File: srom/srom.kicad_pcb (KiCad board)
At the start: 2 copper layers, 83.3 x 76.1 mm, 31 parts, among them J1 Conn_01x03_Female, Q1 PN2222A, SW1 SW_SPST, U1 4075, U2 74LS245, U3 74LS245, U4 74LS245, U5 Pico-rp2040

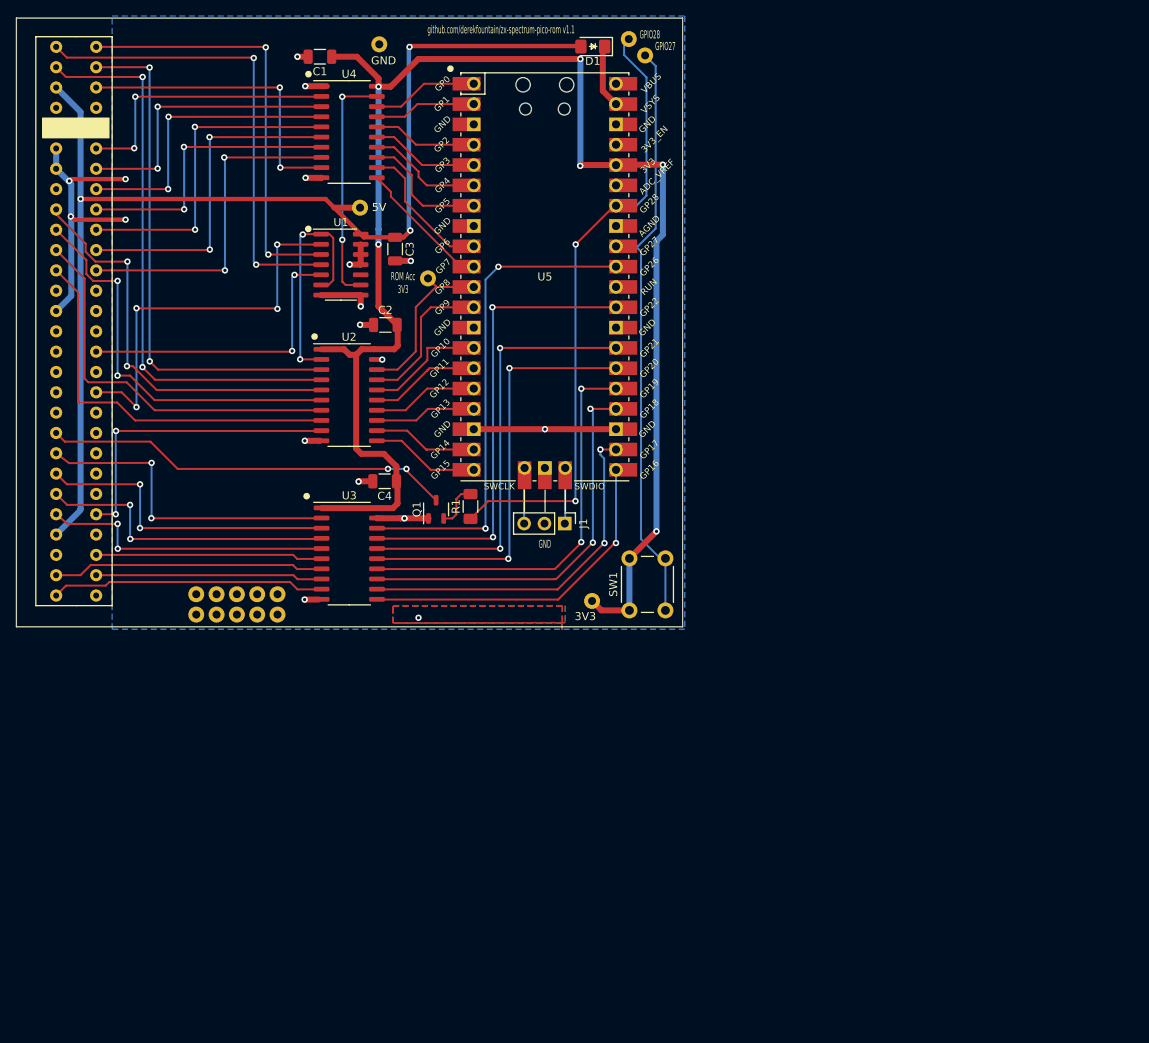
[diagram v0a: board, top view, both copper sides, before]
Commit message: first draft pcb layout
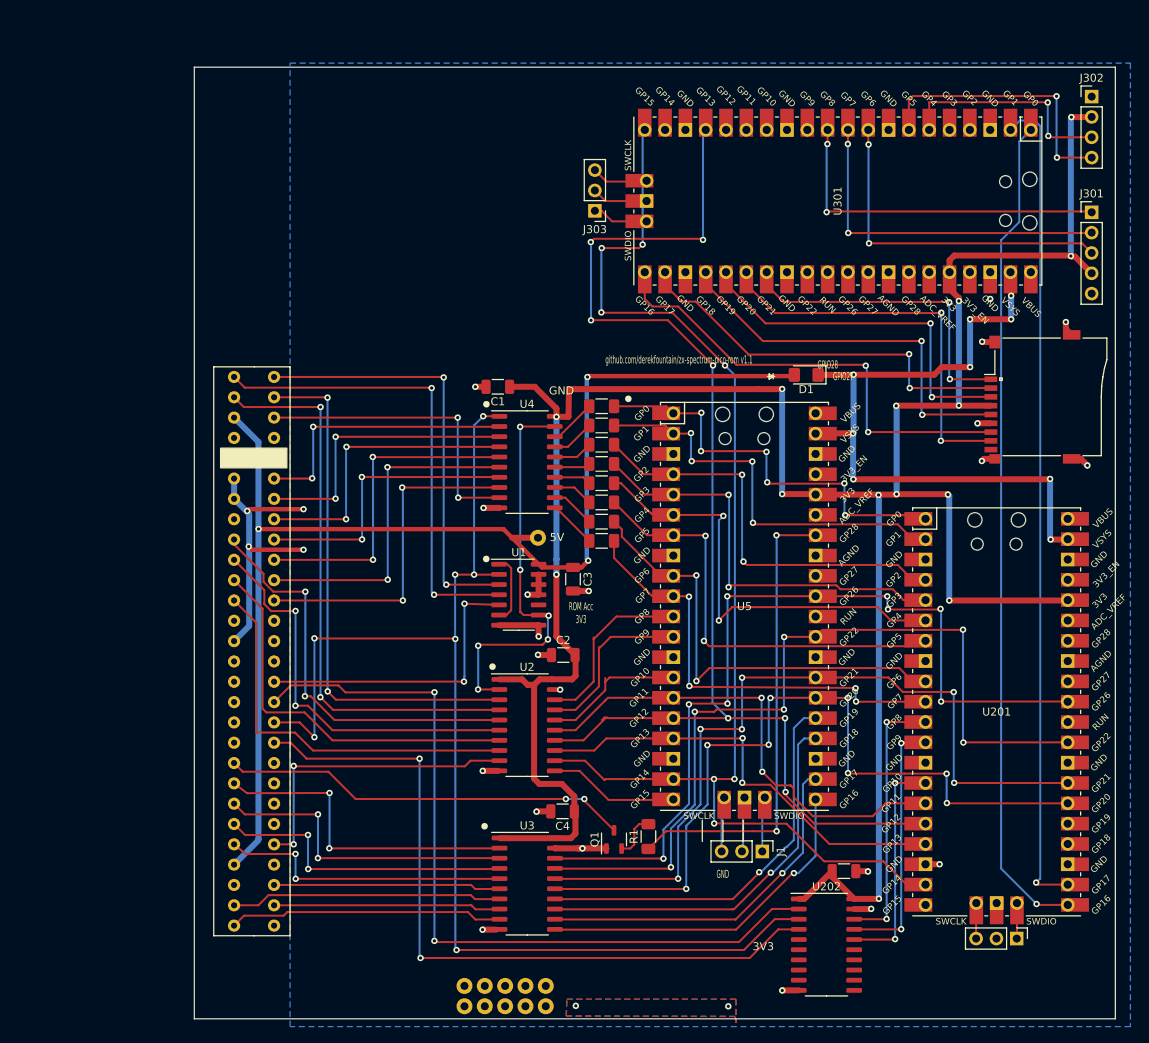
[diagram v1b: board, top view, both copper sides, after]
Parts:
- removed the 14 at (95.1, 122.8)
- removed the 14 at (68.5, 53.3)
- removed the ? at (101.8, 54.6)
- removed the ? at (99.7, 52.6)
- removed the ? at (74.6, 82.5)
- removed SW1: SW_SPST, Button_Switch_THT:SW_PUSH_6mm_H4.3mm
- added C201: C_Small, Capacitor_SMD:C_1206_3216Metric, F.Cu at (126.6, 156.6)
- added J201: Conn_01x03_Female, Connector_PinHeader_2.54mm:PinHeader_1x03_P2.54mm_Vertical, F.Cu at (148.2, 165.0)
- added J301: Conn_01x05_Female, Connector_PinHeader_2.54mm:PinHeader_1x05_P2.54mm_Vertical, F.Cu at (157.6, 74.3)
- added J302: Conn_01x04_Female, Connector_PinHeader_2.54mm:PinHeader_1x04_P2.54mm_Vertical, F.Cu at (157.6, 59.8)
- added J303: Conn_01x03_Female, Connector_PinHeader_2.54mm:PinHeader_1x03_P2.54mm_Vertical, F.Cu at (95.5, 74.1)
- added R101: R470, Resistor_SMD:R_1206_3216Metric_Pad1.30x1.75mm_HandSolder, F.Cu at (96.3, 98.5)
- added R102: R470, Resistor_SMD:R_1206_3216Metric_Pad1.30x1.75mm_HandSolder, F.Cu at (96.3, 100.9)
- added R103: R470, Resistor_SMD:R_1206_3216Metric_Pad1.30x1.75mm_HandSolder, F.Cu at (96.3, 103.3)
- added R104: R470, Resistor_SMD:R_1206_3216Metric_Pad1.30x1.75mm_HandSolder, F.Cu at (96.3, 105.7)
- added R105: R470, Resistor_SMD:R_1206_3216Metric_Pad1.30x1.75mm_HandSolder, F.Cu at (96.3, 108.1)
- added R106: R470, Resistor_SMD:R_1206_3216Metric_Pad1.30x1.75mm_HandSolder, F.Cu at (96.3, 110.5)
- added R107: R470, Resistor_SMD:R_1206_3216Metric_Pad1.30x1.75mm_HandSolder, F.Cu at (96.3, 112.9)
- added R108: R470, Resistor_SMD:R_1206_3216Metric_Pad1.30x1.75mm_HandSolder, F.Cu at (96.3, 115.3)
- added U201: Pico-2 IO, pico-foot:RPi_Pico_SMD_TH, F.Cu at (145.7, 136.7)
- added U202: 74LS245, Package_SO:SO-20_5.3x12.6mm_P1.27mm, F.Cu at (124.4, 165.8)
- added U301: Pico-3 UI, pico-foot:RPi_Pico_SMD_TH, F.Cu at (125.9, 72.8)
- added XS301: 502p_SD_ebay-uSD-push_push_SMD-pak_breakout, uSD:Conn_uSDcard, F.Cu at (155.5, 97.3)
- U5: value Pico-rp2040 -> Pico-1 ROM
- moved 5 59.3 mm to (79.2, 171.0)
- moved 6 59.3 mm to (81.7, 171.0)
- moved 8 59.3 mm to (86.8, 171.0)
- moved 7 59.3 mm to (84.3, 171.0)
- moved 9 59.3 mm to (89.3, 171.0)
- moved 10 59.3 mm to (79.2, 173.5)
- moved 11 59.3 mm to (81.7, 173.5)
- moved 12 59.3 mm to (84.3, 173.5)
- moved 13 59.3 mm to (86.8, 173.5)
- moved 14 59.3 mm to (89.3, 173.5)
- moved D1 49.0 mm to (121.9, 94.6)
- moved U5 48.2 mm to (114.2, 123.5)
- moved J1 47.8 mm to (116.4, 154.2)
- moved U2 46.9 mm to (87.0, 138.4)
- moved C3 46.9 mm to (92.8, 120.1)
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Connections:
- net Net-(D1-Pad1) renamed PICO_PWR
- net ROM_ACCESS_INV_3V3 renamed ROM_READ_INV_3V3
- net SWDCLK renamed SWDCLK_P1
- net SWDIO renamed SWDIO_P1
- U1 pad 11: GND -> unconnected-(U1-Pad11)
- U1 pad 12: GND -> unconnected-(U1-Pad12)
- U1 pad 13: GND -> unconnected-(U1-Pad13)
- U2 pad 2: ROM_ACCESS_INV -> ROM_READ_INV
- U4 pad 1: GND -> ZXRD
- U4 pad 11: D7 -> Net-(R108-Pad1)
- U4 pad 12: D4 -> Net-(R107-Pad1)
- U4 pad 13: D6 -> Net-(R106-Pad1)
- U4 pad 14: D3 -> Net-(R105-Pad1)
- U4 pad 15: D5 -> Net-(R104-Pad1)
- U4 pad 16: D2 -> Net-(R103-Pad1)
- U4 pad 17: D1 -> Net-(R102-Pad1)
- U4 pad 18: D0 -> Net-(R101-Pad1)
- U4 pad 19: ROM_READ_INV -> GND
- U5 pad 32: PICO_USER_INPUT -> unconnected-(U5-Pad32)
- Z1 pad A17: unconnected-(Z1-PadA17) -> ZXIORQ
- Z1 pad A19: unconnected-(Z1-PadA19) -> ZXWR
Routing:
- net A1: track 13.2 -> 160.8 mm, vias 0 -> 7
- net A3: track 13.2 -> 158.3 mm, vias 0 -> 7
- net +3V3: track 196.8 -> 321.7 mm, vias 6 -> 14
- net ZXRD: track 49.1 -> 155.4 mm, vias 4 -> 7
- net UI_PICO_TX: track 0.00 -> 104.1 mm, vias 0 -> 1
- net UI_PICO_RX: track 0.00 -> 103.3 mm, vias 0 -> 1
- net ZXIORQ: track 0.00 -> 99.7 mm, vias 0 -> 2
- net ZXWR: track 0.00 -> 92.9 mm, vias 0 -> 2
- net PICO_PWR: track 7.87 -> 88.6 mm, vias 0 -> 9
- net PICO_USER_INPUT: track 75.5 -> 0.00 mm
- net MISO_D0: track 0.00 -> 58.5 mm, vias 0 -> 2
- net SD_SS: track 0.00 -> 50.2 mm, vias 0 -> 2
- net SD_DAT1: track 0.00 -> 49.7 mm, vias 0 -> 2
- net SD_CLK: track 0.00 -> 49.3 mm, vias 0 -> 2
- net A4: track 53.6 -> 101.3 mm, vias 2 -> 8
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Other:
- board size 83.3 x 76.1 mm -> 115.1 x 118.9 mm

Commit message: design rules checker happy
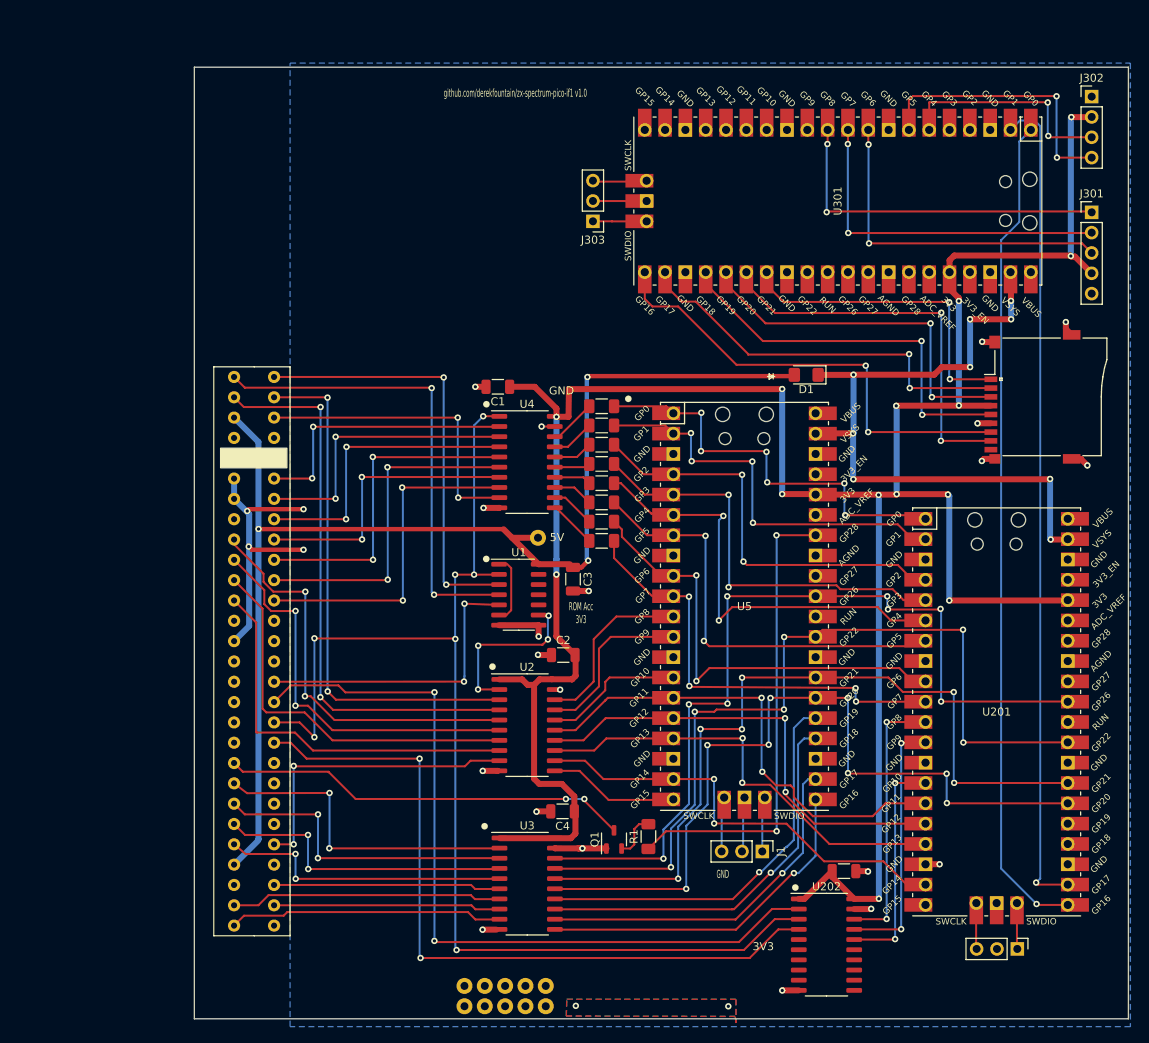
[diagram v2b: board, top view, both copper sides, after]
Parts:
- moved J303 1.33 mm to (95.2, 75.4)
- moved J201 1.30 mm to (148.3, 166.3)
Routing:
- net A3: track 158.3 -> 53.6 mm, vias 7 -> 2
- net A1: track 160.8 -> 58.5 mm, vias 7 -> 2
- net GND: track 122.4 -> 93.8 mm, vias 28 -> 26
- net unconnected-(U1-Pad12): track 3.92 -> 0.00 mm, vias 1 -> 0
- net D4: track 56.9 -> 53.7 mm
- net +3V3: track 321.7 -> 319.1 mm
- net A4: track 101.3 -> 99.4 mm
- net SD_SS: track 50.2 -> 48.6 mm
- net SD_DAT2: track 40.1 -> 38.5 mm
- net D2: track 52.2 -> 50.6 mm
- net D1: track 51.3 -> 49.7 mm
- net OLED_SDA: track 34.4 -> 32.9 mm
- net SD_DAT1: track 49.7 -> 48.2 mm
- net SD_CLK: track 49.3 -> 47.8 mm
- net MOSI_DI: track 45.7 -> 44.3 mm
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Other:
- board size 115.1 x 118.9 mm -> 116.8 x 118.9 mm
- board text added: "github.com/derekfountain/zx-spectrum-pico-if1 v1.0"
- board text removed: "GPIO27"
- board text removed: "GPIO28"
- board text removed: "github.com/derekfountain/zx-spectrum-pico-rom v1.1"

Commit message: ready for fab
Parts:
- added 10: , , F.Cu at (84.7, 92.5)
- added 10: , , F.Cu at (84.7, 87.6)
- added 10: , , F.Cu at (133.0, 173.3)
- added 10: , , F.Cu at (149.8, 173.3)
- added 10: , , F.Cu at (84.7, 82.5)
- added 11: , , F.Cu at (152.3, 173.3)
- added 11: , , F.Cu at (135.6, 173.3)
- added 11: , , F.Cu at (87.3, 87.6)
- added 11: , , F.Cu at (87.2, 82.5)
- added 11: , , F.Cu at (87.2, 92.5)
- added 12: , , F.Cu at (154.8, 173.3)
- added 12: , , F.Cu at (89.8, 82.5)
- added 12: , , F.Cu at (138.1, 173.3)
- added 12: , , F.Cu at (89.8, 87.6)
- added 12: , , F.Cu at (89.8, 92.5)
- added 13: , , F.Cu at (92.3, 87.6)
- added 13: , , F.Cu at (157.4, 173.3)
- added 13: , , F.Cu at (92.3, 92.5)
- added 13: , , F.Cu at (140.6, 173.3)
- added 13: , , F.Cu at (92.3, 82.5)
- added 14: , , F.Cu at (94.8, 82.5)
- added 14: , , F.Cu at (94.8, 92.5)
- added 14: , , F.Cu at (94.9, 87.6)
- added 14: , , F.Cu at (143.2, 173.3)
- added 14: , , F.Cu at (159.9, 173.3)
- added 5: , , F.Cu at (84.7, 90.0)
- added 5: , , F.Cu at (149.8, 170.7)
- added 5: , , F.Cu at (133.0, 170.8)
- added 5: , , F.Cu at (84.7, 80.0)
- added 5: , , F.Cu at (84.7, 85.0)
- added 6: , , F.Cu at (87.2, 80.0)
- added 6: , , F.Cu at (135.6, 170.8)
- added 6: , , F.Cu at (87.2, 90.0)
- added 6: , , F.Cu at (87.3, 85.0)
- added 6: , , F.Cu at (152.3, 170.7)
- added 7: , , F.Cu at (89.8, 80.0)
- added 7: , , F.Cu at (154.8, 170.7)
- added 7: , , F.Cu at (89.8, 85.0)
- added 7: , , F.Cu at (138.1, 170.8)
- added 7: , , F.Cu at (89.8, 90.0)
- added 8: , , F.Cu at (92.3, 85.0)
- added 8: , , F.Cu at (92.3, 90.0)
- added 8: , , F.Cu at (140.6, 170.8)
- added 8: , , F.Cu at (157.4, 170.7)
- added 8: , , F.Cu at (92.3, 80.0)
- added 9: , , F.Cu at (94.8, 90.0)
- added 9: , , F.Cu at (159.9, 170.7)
- added 9: , , F.Cu at (94.9, 85.0)
- added 9: , , F.Cu at (143.2, 170.8)
- added 9: , , F.Cu at (94.8, 80.0)
- added ?: , , F.Cu at (132.8, 167.7)
- added ?: , , F.Cu at (159.1, 108.5)
- added ?: , , F.Cu at (136.0, 167.7)
- added ?: , , F.Cu at (158.3, 164.8)
- added ?: , , F.Cu at (152.2, 167.8)
- added ?: , , F.Cu at (138.9, 167.8)
- added ?: , , F.Cu at (152.3, 164.9)
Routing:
- net +3V3: track 319.1 -> 337.3 mm
- net IORQ: track 33.5 -> 42.5 mm
- net UI_PICO_RX: track 103.3 -> 111.5 mm
- net UI_PICO_TX: track 104.1 -> 108.9 mm
- net RD: track 32.2 -> 36.7 mm
- net WR: track 28.4 -> 31.1 mm
- net A2: track 55.8 -> 56.4 mm
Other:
- board text added: "IORQ"
- board text added: "RD"
- board text added: "RX"
- board text added: "TX"
- board text added: "WR"

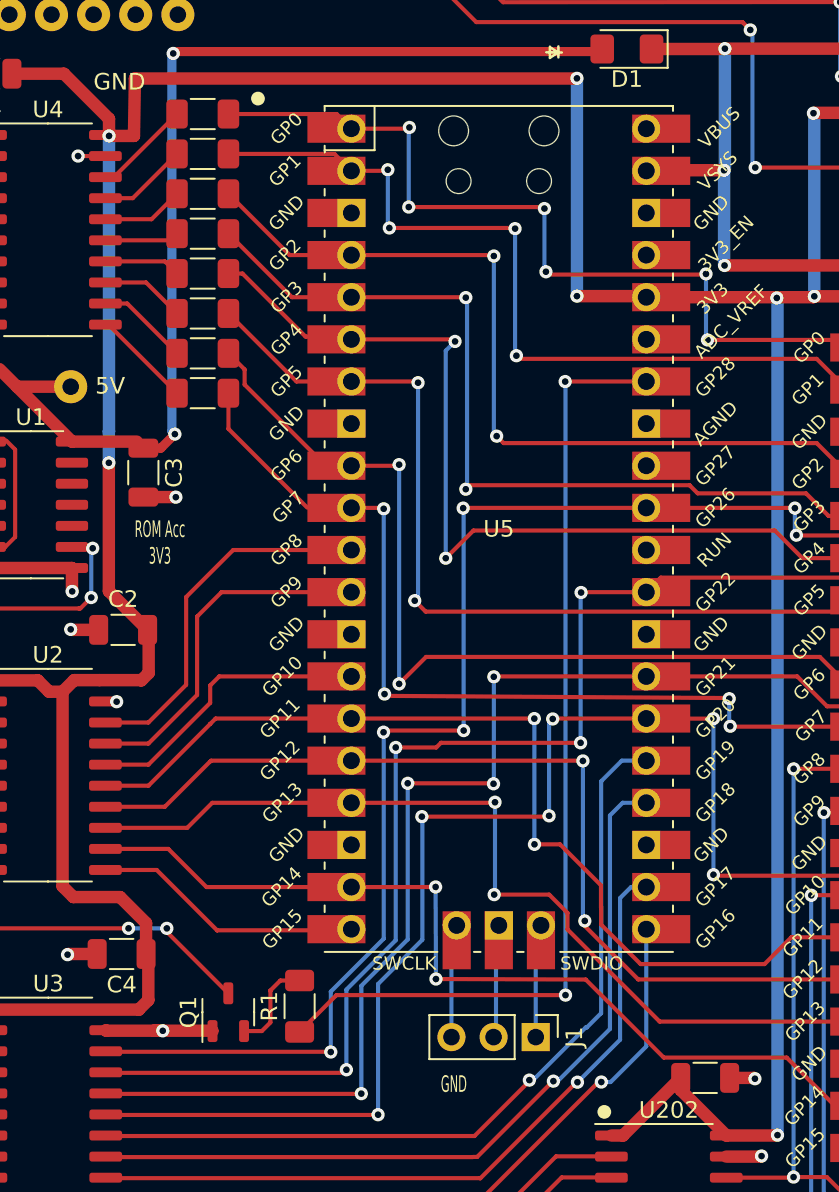
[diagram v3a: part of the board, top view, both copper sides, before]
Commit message: fix 2222 transistor footprint on PCB
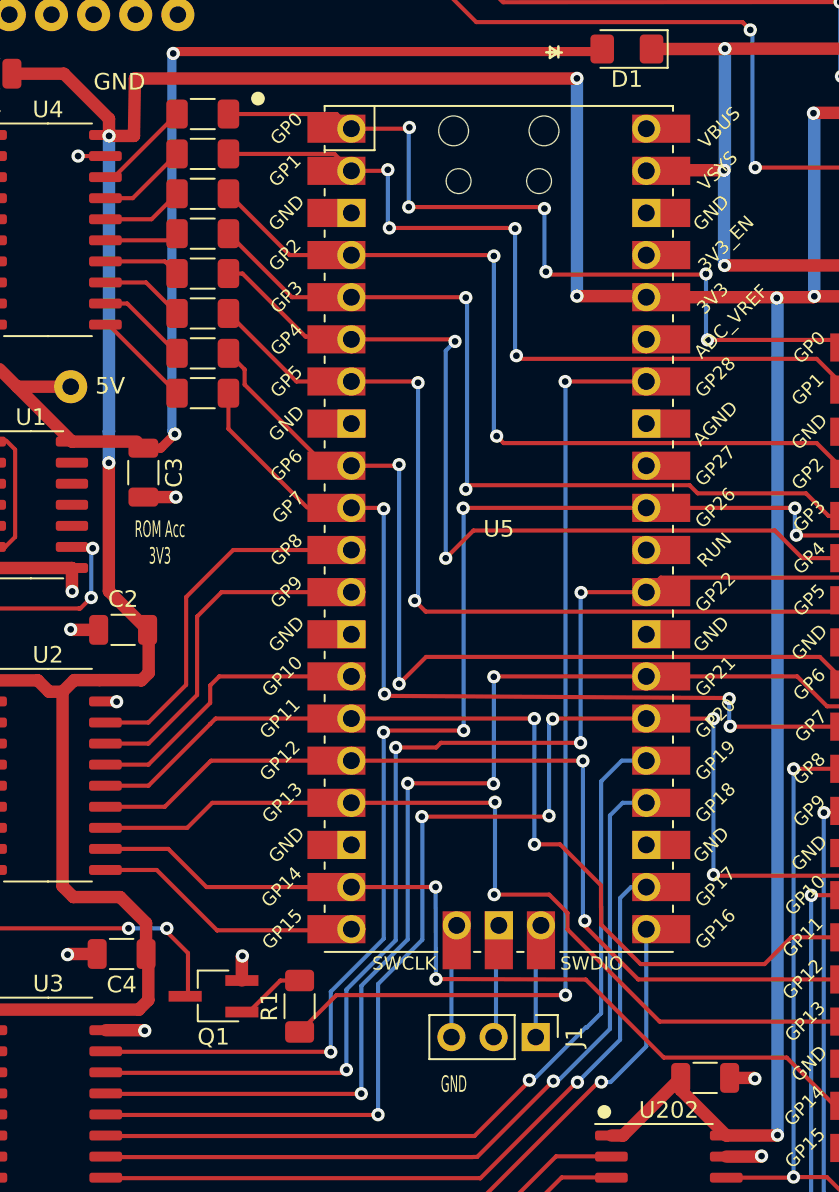
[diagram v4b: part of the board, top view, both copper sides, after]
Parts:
- Q1: value PN2222A -> PMBT2222A; footprint Package_TO_SOT_SMD:SOT-23-3 -> Package_TO_SOT_SMD:TSOT-23_HandSoldering
- moved Q1 1.31 mm to (97.0, 151.7), turned to 180 degrees
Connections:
- Q1 pad 1: GND -> Net-(R1-Pad2)
- Q1 pad 2: Net-(Q1-Pad2) -> GND
- R1 pad 2: Net-(Q1-Pad2) -> Net-(R1-Pad2)
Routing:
- net Net-(Q1-Pad2): track 5.75 -> 0.00 mm
- net Net-(R1-Pad2): track 0.00 -> 4.27 mm
- net GND: track 93.8 -> 90.6 mm, vias 26 -> 27
- net ZXRESET: track 51.1 -> 50.3 mm
